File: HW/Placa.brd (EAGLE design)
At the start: 160 x 100 mm, 28 parts, among them IC1 7805TV, T1 BC846, T2 BC846, T3 BC846

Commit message: Correcciones SCH
Algunas correcciones, falta revisión final.
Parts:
- removed C6, C7, C8: 100uF x16v, resistor:C025-025X050
- added C10, C11, C12, C13: 47uF x 16V, rcl:E2,5-6E
- added C9: 47uF x 25V, rcl:E2,5-6E
- C1: value 0,1u -> 100nF
- C2, C3: value 47u -> 100nF
- IC1: value 7805TV -> LM2940
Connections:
- removed net N$11: R8.1, T3.3
- net GND: now also C10.-, C11.-, C12.-, C13.-, C9.-, CENTRAL.4; no longer C6.2, C7.2, C8.2, CENTRAL.2
- net N$1: now also C9.+
- net N$2: now also CENTRAL.2; no longer CENTRAL.3
- net N$3: now also CENTRAL.3; no longer CENTRAL.4
- net N$7: now also C11.+; no longer C6.1
- net N$8: now also C12.+; no longer C7.1
- net N$9: now also C13.+; no longer C8.1
- net SENSOR1: no longer R6.2
- net SENSOR2: no longer R7.2
- net SENSOR3: now also R8.1, T3.3; no longer R8.2
- net VCC: now also C10.+, R6.2, R7.2, R8.2

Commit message: Proyect Board
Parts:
- removed C10, C11, C12, C13: 47uF x 16V, rcl:E2,5-6E
- removed C9: 47uF x 25V, rcl:E2,5-6E
- added C6, C7, C8: 100uF x16v, resistor:C025-025X050
- C1: value 100nF -> 0,1u
- C2, C3: value 100nF -> 47u
- IC1: value LM2940 -> 7805TV
- moved D1 78.9 mm to (91.6, 26.5), turned to 180 degrees
- moved D3 72.6 mm to (91.5, 33.4), turned to 180 degrees
- moved D2 69.6 mm to (91.5, 29.9), turned to 180 degrees
- moved C3 60.4 mm to (98.0, 69.2)
- moved C2 57.2 mm to (88.1, 69.2)
- moved IC1 51.8 mm to (94.8, 76.3)
- moved SENSOR 44.9 mm to (74.9, 31.8)
- moved SV1 41.9 mm to (56.2, 47.8), turned to 270 degrees
- moved R4 41.2 mm to (43.6, 67.7)
- moved CENTRAL 40.3 mm to (74.9, 61.0)
- moved R5 37.8 mm to (51.4, 59.9)
- moved R3 35.2 mm to (45.3, 71.9)
- moved R6 35.0 mm to (51.7, 73.3), turned to 180 degrees
- moved R2 34.6 mm to (81.1, 64.7), turned to 180 degrees
- moved C4 33.6 mm to (88.7, 54.1)
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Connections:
- new net N$11: R8.1, T3.3
- net GND: now also C6.2, C7.2, C8.2, CENTRAL.2; no longer C10.-, C11.-, C12.-, C13.-, C9.-, CENTRAL.4
- net N$1: no longer C9.+
- net N$2: now also CENTRAL.3; no longer CENTRAL.2
- net N$3: now also CENTRAL.4; no longer CENTRAL.3
- net N$7: now also C6.1; no longer C11.+
- net N$8: now also C7.1; no longer C12.+
- net N$9: now also C8.1; no longer C13.+
- net SENSOR1: now also R6.2
- net SENSOR2: now also R7.2
- net SENSOR3: now also R8.2; no longer R8.1, T3.3
- net VCC: no longer C10.+, R6.2, R7.2, R8.2
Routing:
- net GND: track 0.00 -> 183.9 mm
- net VCC: track 0.00 -> 152.9 mm
- net RST: track 0.00 -> 121.9 mm
- net TXD: track 0.00 -> 49.5 mm
- net N$1: track 0.00 -> 45.2 mm
- net RXD: track 0.00 -> 36.4 mm
- net CONTROL485: track 0.00 -> 31.8 mm
- net BKGD: track 0.00 -> 31.5 mm
- net N$2: track 0.00 -> 25.4 mm
- net N$4: track 0.00 -> 24.3 mm
- net N$5: track 0.00 -> 18.4 mm
- net N$6: track 0.00 -> 13.3 mm
- net N$3: track 0.00 -> 12.4 mm
- net N$9: track 0.00 -> 5.12 mm
- net N$8: track 0.00 -> 4.54 mm
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
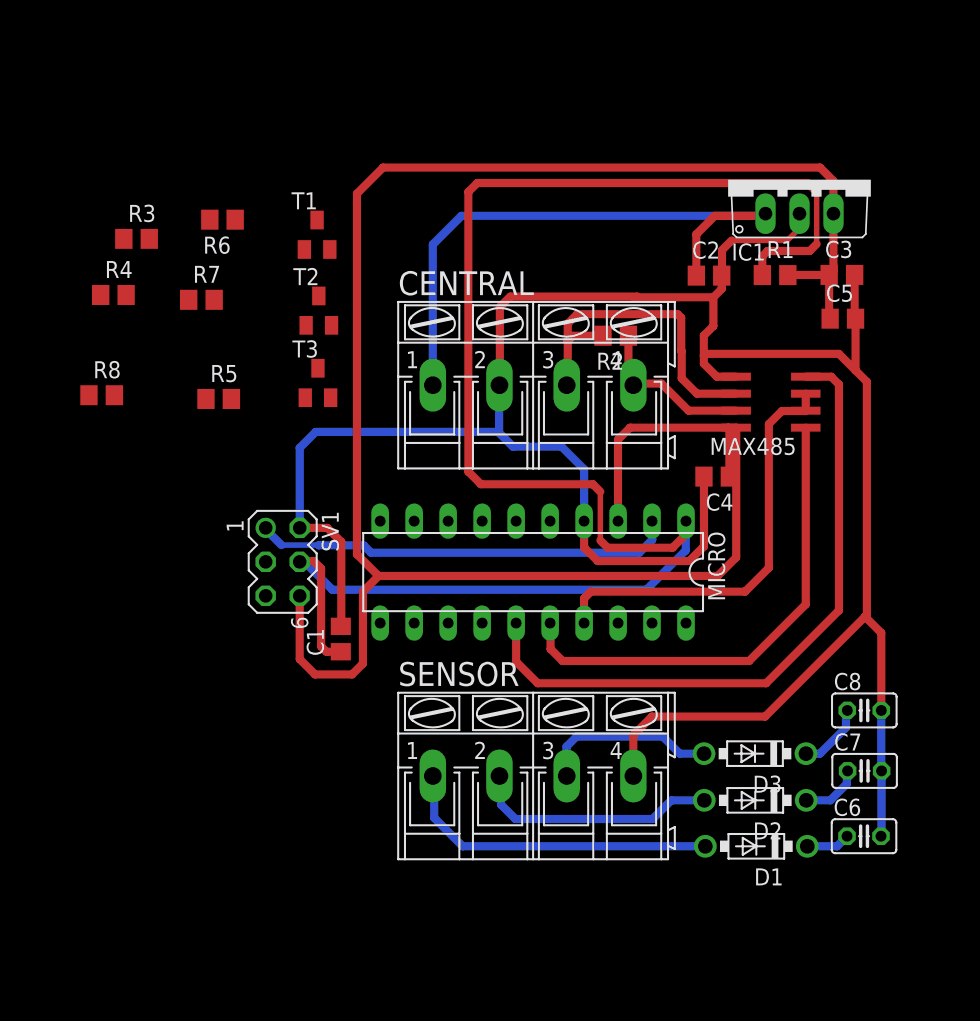
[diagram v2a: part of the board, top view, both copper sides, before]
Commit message: Proyecto Eagle
Esquematico terminado
Board falta corregir errores
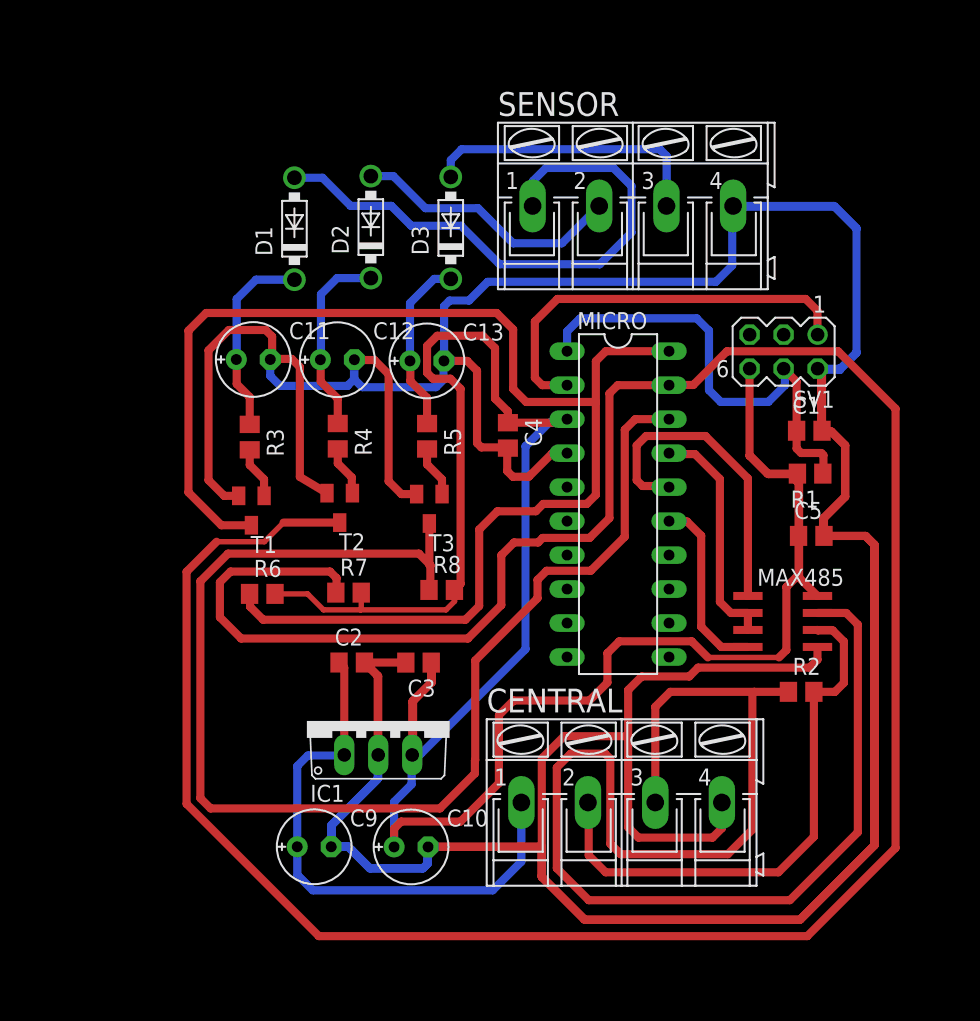
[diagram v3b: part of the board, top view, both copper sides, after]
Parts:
- removed C6, C7, C8: 100uF x16v, resistor:C025-025X050
- added C10, C11, C12, C13: 47uF x 16V, rcl:E2,5-6E
- added C9: 47uF x 25V, rcl:E2,5-6E
- C1: value 0,1u -> 100nF
- C2, C3: value 47u -> 100nF
- IC1: value 7805TV -> LM2940
- moved D1 57.6 mm to (57.1, 72.7), turned to 90 degrees
- moved D2 51.6 mm to (62.8, 72.8), turned to 90 degrees
- moved IC1 51.3 mm to (63.4, 35.9)
- moved D3 45.4 mm to (68.8, 72.7), turned to 90 degrees
- moved SENSOR 43.3 mm to (82.4, 74.4)
- moved C3 42.9 mm to (66.4, 40.2), turned to 180 degrees
- moved SV1 40.6 mm to (93.7, 63.5), turned to 180 degrees
- moved C2 39.4 mm to (61.4, 40.2)
- moved C1 38.3 mm to (95.6, 57.6), turned to 0 degrees
- moved CENTRAL 31.9 mm to (81.5, 29.8)
- moved R2 30.0 mm to (95.0, 38.0), turned to 0 degrees
- moved R8 29.3 mm to (68.1, 45.7)
- moved R6 28.1 mm to (54.7, 45.4), turned to 0 degrees
- moved R7 24.5 mm to (61.1, 45.5)
- moved T1 21.2 mm to (53.9, 51.6), turned to 180 degrees
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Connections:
- removed net N$11: R8.1, T3.3
- removed net N$13: R7.1, T2.3
- removed net N$15: R6.1, T1.3
- net GND: now also C10.-, C11.-, C12.-, C13.-, C9.-, CENTRAL.4; no longer C6.2, C7.2, C8.2, CENTRAL.2
- net N$1: now also C9.+
- net N$2: now also CENTRAL.2; no longer CENTRAL.3
- net N$3: now also CENTRAL.3; no longer CENTRAL.4
- net N$7: now also C11.+; no longer C6.1
- net N$8: now also C12.+; no longer C7.1
- net N$9: now also C13.+; no longer C8.1
- net SENSOR1: now also R6.1, T1.3; no longer R6.2
- net SENSOR2: now also R7.1, T2.3; no longer R7.2
- net SENSOR3: now also R8.1, T3.3; no longer R8.2
- net VCC: now also C10.+, R6.2, R7.2, R8.2
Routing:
- net GND: track 183.9 -> 414.0 mm, vias 0 -> 3
- net SENSOR2: track 0.00 -> 205.4 mm
- net SENSOR1: track 0.00 -> 104.4 mm
- net SENSOR3: track 0.00 -> 97.5 mm
- net N$3: track 12.4 -> 102.6 mm
- net RST: track 121.9 -> 35.1 mm
- net TXD: track 49.5 -> 13.8 mm
- net VCC: track 152.9 -> 185.7 mm, vias 0 -> 1
- net N$4: track 24.3 -> 42.5 mm
- net N$2: track 25.4 -> 41.2 mm
- net CONTROL485: track 31.8 -> 17.5 mm
- net RXD: track 36.4 -> 23.9 mm
- net N$7: track 3.28 -> 14.7 mm
- net N$8: track 4.54 -> 14.4 mm
- net N$6: track 13.3 -> 21.7 mm
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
